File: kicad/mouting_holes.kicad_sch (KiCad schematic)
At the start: 6 parts, among them J1 Spacer M2, J2 Spacer M2, J3 Screw M2, J4 Screw M2, J5 Screw M2, J6 Screw M2

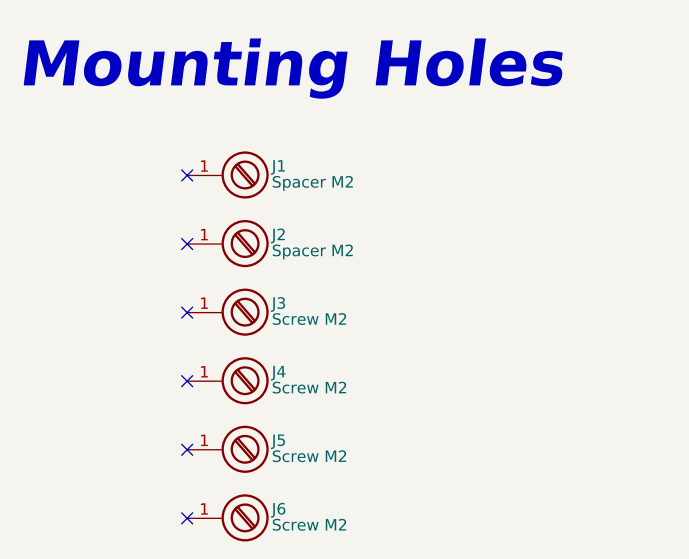
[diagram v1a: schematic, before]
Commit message: Add voltage value to caps, update BOM, SCH, ASM
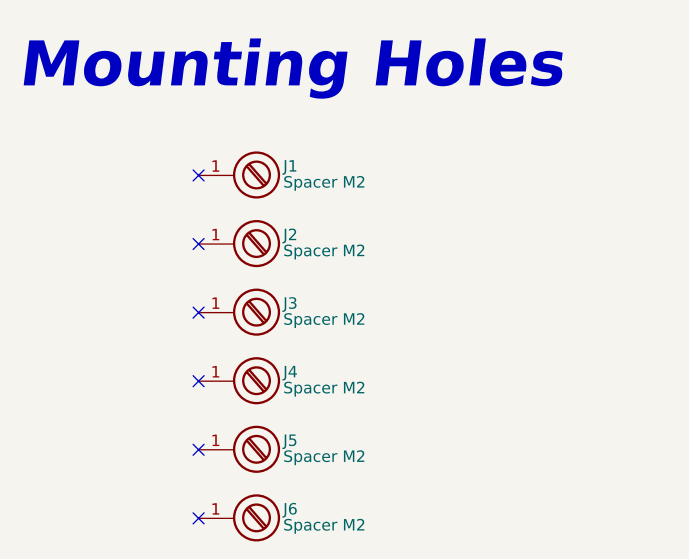
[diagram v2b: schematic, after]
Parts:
- J3, J4, J5, J6: value Screw M2 -> Spacer M2
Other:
- moved on the sheet: J1, J2, J3, J4, J5, J6
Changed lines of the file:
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@@
 (kicad_sch (version 20211123) (generator eeschema)
   (paper "A4")
-  (no_connect (at 146.05 93.98))
-  (no_connect (at 146.05 116.8399))
-  (no_connect (at 146.05 101.5999))
-  (no_connect (at 146.05 86.3599))
-  (no_connect (at 146.05 109.22))
-  (no_connect (at 146.05 78.74))
+  (no_connect (at 147.32 93.98))
+  (no_connect (at 147.32 116.84))
+  (no_connect (at 147.32 101.6))
+  (no_connect (at 147.32 86.36))
+  (no_connect (at 147.32 109.22))
+  (no_connect (at 147.32 78.74))
   (text "Mounting Holes" (at 127.254 69.596 0)
     (effects (font (size 5 5) (thickness 1.0008) bold italic) (justify left bottom))
   )
-  (symbol (lib_id "Mechanical:Screw_Terminal_01x01") (at 152.4878 86.3094 0) (unit 1)
+  (symbol (lib_id "Mechanical:Screw_Terminal_01x01") (at 153.7578 86.3095 0) (unit 1)
     (in_bom yes) (on_board yes)
-    (property "Reference" "J2" (id 0) (at 155.448 85.3439 0)
+    (property "Reference" "J2" (id 0) (at 156.718 85.344 0)
       (effects (font (size 1.27 1.27)) (justify left))
     )
-    (property "Value" "Spacer M2" (id 1) (at 155.448 87.1219 0)
+    (property "Value" "Spacer M2" (id 1) (at 156.718 87.122 0)
       (effects (font (size 1.27 1.27)) (justify left))
     )
-    (property "Footprint" "MountingHole:MountingHole_2.2mm_M2_DIN965_Pad" (id 2) (at 152.4878 86.3094 0)
+    (property "Footprint" "MountingHole:MountingHole_2.2mm_M2_DIN965_Pad" (id 2) (at 153.7578 86.3095 0)
       (effects (font (size 1.27 1.27)) hide)
     )
-    (property "Datasheet" "~" (id 3) (at 152.4878 86.3094 0)
+    (property "Datasheet" "~" (id 3) (at 153.7578 86.3095 0)
       (effects (font (size 1.27 1.27)) hide)
     )
     (pin "1")
   )
-  (symbol (lib_id "Mechanical:Screw_Terminal_01x01") (at 152.4878 116.7894 0) (unit 1)
+  (symbol (lib_id "Mechanical:Screw_Terminal_01x01") (at 153.7578 116.7895 0) (unit 1)
     (in_bom yes) (on_board yes)
-    (property "Reference" "J6" (id 0) (at 155.448 115.8239 0)
+    (property "Reference" "J6" (id 0) (at 156.718 115.824 0)
       (effects (font (size 1.27 1.27)) (justify left))
     )
-    (property "Value" "Screw M2" (id 1) (at 155.448 117.6019 0)
+    (property "Value" "Spacer M2" (id 1) (at 156.718 117.602 0)
       (effects (font (size 1.27 1.27)) (justify left))
     )
-    (property "Footprint" "MountingHole:MountingHole_2.2mm_M2_DIN965_Pad" (id 2) (at 152.4878 116.7894 0)
+    (property "Footprint" "MountingHole:MountingHole_2.2mm_M2_DIN965_Pad" (id 2) (at 153.7578 116.7895 0)
       (effects (font (size 1.27 1.27)) hide)
     )
-    (property "Datasheet" "~" (id 3) (at 152.4878 116.7894 0)
+    (property "Datasheet" "~" (id 3) (at 153.7578 116.7895 0)
       (effects (font (size 1.27 1.27)) hide)
     )
     (pin "1")
   )
-  (symbol (lib_id "Mechanical:Screw_Terminal_01x01") (at 152.4878 78.6895 0) (unit 1)
+  (symbol (lib_id "Mechanical:Screw_Terminal_01x01") (at 153.7578 78.6895 0) (unit 1)
     (in_bom yes) (on_board yes)
-    (property "Reference" "J1" (id 0) (at 155.448 77.724 0)
+    (property "Reference" "J1" (id 0) (at 156.718 77.724 0)
       (effects (font (size 1.27 1.27)) (justify left))
     )
-    (property "Value" "Spacer M2" (id 1) (at 155.448 79.502 0)
+    (property "Value" "Spacer M2" (id 1) (at 156.718 79.502 0)
       (effects (font (size 1.27 1.27)) (justify left))
     )
-    (property "Footprint" "MountingHole:MountingHole_2.2mm_M2_DIN965_Pad" (id 2) (at 152.4878 78.6895 0)
+    (property "Footprint" "MountingHole:MountingHole_2.2mm_M2_DIN965_Pad" (id 2) (at 153.7578 78.6895 0)
       (effects (font (size 1.27 1.27)) hide)
     )
-    (property "Datasheet" "~" (id 3) (at 152.4878 78.6895 0)
+    (property "Datasheet" "~" (id 3) (at 153.7578 78.6895 0)
       (effects (font (size 1.27 1.27)) hide)
     )
     (pin "1")
   )
-  (symbol (lib_id "Mechanical:Screw_Terminal_01x01") (at 152.4878 93.9295 0) (unit 1)
+  (symbol (lib_id "Mechanical:Screw_Terminal_01x01") (at 153.7578 93.9295 0) (unit 1)
     (in_bom yes) (on_board yes)
-    (property "Reference" "J3" (id 0) (at 155.448 92.964 0)
+    (property "Reference" "J3" (id 0) (at 156.718 92.964 0)
       (effects (font (size 1.27 1.27)) (justify left))
     )
-    (property "Value" "Screw M2" (id 1) (at 155.448 94.742 0)
+    (property "Value" "Spacer M2" (id 1) (at 156.718 94.742 0)
       (effects (font (size 1.27 1.27)) (justify left))
     )
-    (property "Footprint" "MountingHole:MountingHole_2.2mm_M2_DIN965_Pad" (id 2) (at 152.4878 93.9295 0)
+    (property "Footprint" "MountingHole:MountingHole_2.2mm_M2_DIN965_Pad" (id 2) (at 153.7578 93.9295 0)
       (effects (font (size 1.27 1.27)) hide)
     )
-    (property "Datasheet" "~" (id 3) (at 152.4878 93.9295 0)
+    (property "Datasheet" "~" (id 3) (at 153.7578 93.9295 0)
       (effects (font (size 1.27 1.27)) hide)
     )
     (pin "1")
   )
-  (symbol (lib_id "Mechanical:Screw_Terminal_01x01") (at 152.4878 101.5494 0) (unit 1)
+  (symbol (lib_id "Mechanical:Screw_Terminal_01x01") (at 153.7578 101.5495 0) (unit 1)
     (in_bom yes) (on_board yes)
-    (property "Reference" "J4" (id 0) (at 155.448 100.5839 0)
+    (property "Reference" "J4" (id 0) (at 156.718 100.584 0)
       (effects (font (size 1.27 1.27)) (justify left))
     )
-    (property "Value" "Screw M2" (id 1) (at 155.448 102.3619 0)
+    (property "Value" "Spacer M2" (id 1) (at 156.718 102.362 0)
       (effects (font (size 1.27 1.27)) (justify left))
     )
-    (property "Footprint" "MountingHole:MountingHole_2.2mm_M2_DIN965_Pad" (id 2) (at 152.4878 101.5494 0)
+    (property "Footprint" "MountingHole:MountingHole_2.2mm_M2_DIN965_Pad" (id 2) (at 153.7578 101.5495 0)
       (effects (font (size 1.27 1.27)) hide)
     )
-    (property "Datasheet" "~" (id 3) (at 152.4878 101.5494 0)
+    (property "Datasheet" "~" (id 3) (at 153.7578 101.5495 0)
       (effects (font (size 1.27 1.27)) hide)
     )
     (pin "1")
   )
-  (symbol (lib_id "Mechanical:Screw_Terminal_01x01") (at 152.4878 109.1695 0) (unit 1)
+  (symbol (lib_id "Mechanical:Screw_Terminal_01x01") (at 153.7578 109.1695 0) (unit 1)
     (in_bom yes) (on_board yes)
-    (property "Reference" "J5" (id 0) (at 155.448 108.204 0)
+    (property "Reference" "J5" (id 0) (at 156.718 108.204 0)
       (effects (font (size 1.27 1.27)) (justify left))
     )
-    (property "Value" "Screw M2" (id 1) (at 155.448 109.982 0)
+    (property "Value" "Spacer M2" (id 1) (at 156.718 109.982 0)
       (effects (font (size 1.27 1.27)) (justify left))
     )
-    (property "Footprint" "MountingHole:MountingHole_2.2mm_M2_DIN965_Pad" (id 2) (at 152.4878 109.1695 0)
+    (property "Footprint" "MountingHole:MountingHole_2.2mm_M2_DIN965_Pad" (id 2) (at 153.7578 109.1695 0)
       (effects (font (size 1.27 1.27)) hide)
     )
-    (property "Datasheet" "~" (id 3) (at 152.4878 109.1695 0)
+    (property "Datasheet" "~" (id 3) (at 153.7578 109.1695 0)
       (effects (font (size 1.27 1.27)) hide)
     )

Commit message: Add wiring diagram; Add work ours (stage 2); refactor folders
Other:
- title: (none) -> RadioSens v1
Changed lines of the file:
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@@
 (kicad_sch (version 20211123) (generator eeschema)
   (paper "A4")
+  (title_block
+    (title "RadioSens v1")
+    (comment 2 "Electrical Circuit")
+  )
   (no_connect (at 147.32 93.98))
   (no_connect (at 147.32 116.84))
